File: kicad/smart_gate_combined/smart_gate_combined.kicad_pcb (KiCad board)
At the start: 2 copper layers, 250 x 150 mm, 35 parts

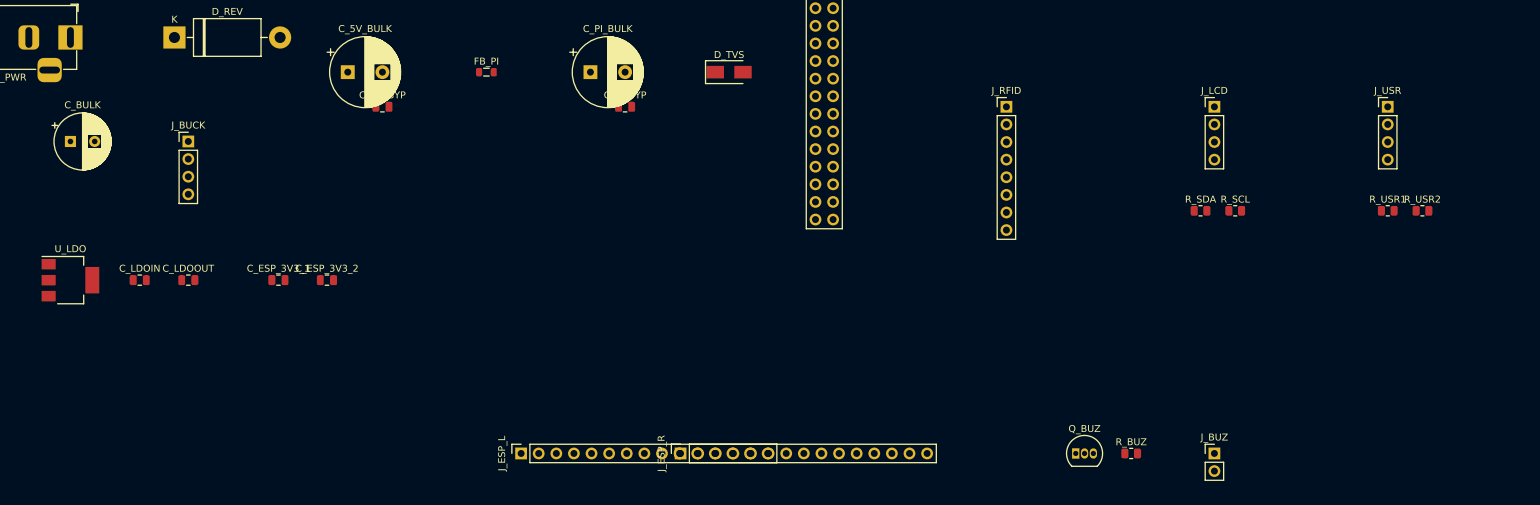
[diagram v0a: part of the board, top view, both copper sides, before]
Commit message: fix(kicad): Pi 4 target + all-THT footprints
Two clarifications from user 2026-05-22:
1. Hardware is Raspberry Pi 4 (not Pi 5 as previously assumed). GPIO layout
   identical, but power budget relaxed (1.5A peak vs 5A) and Pi 4 has no
   strict PMIC so GPIO-fed 5V is safer.
2. All discrete components must be through-hole (THT), not SMD — user does
   not have reflow/hot-air, prefers hand-soldering.

Changes:
- Spec §1, §2, decision log: Pi 5 -> Pi 4, buck 5A -> 3A, peak 3.6A -> 2.1A
- Spec §2: AMS1117 SOT-223 -> LM1117-3.3 TO-220
- Spec risks 6: Pi 4 tolerance noted (more forgiving than Pi 5)
- Spec decisions 23-24: THT preference + Pi 4 target documented
- SKiDL build_combined.py: all SMD footprints converted to THT
  (R 0805 -> Axial DIN0207, C 0805 -> Disc D5.0, D_SMA -> DO-15,
   AMS1117 -> LM1117-3.3 TO-220, L 0805 -> Axial Fastron)
- Regenerated netlist + PCB: 35 footprints, 0 ERC errors

Co-Authored-By: Claude Opus 4.7 <noreply@anthropic.com>
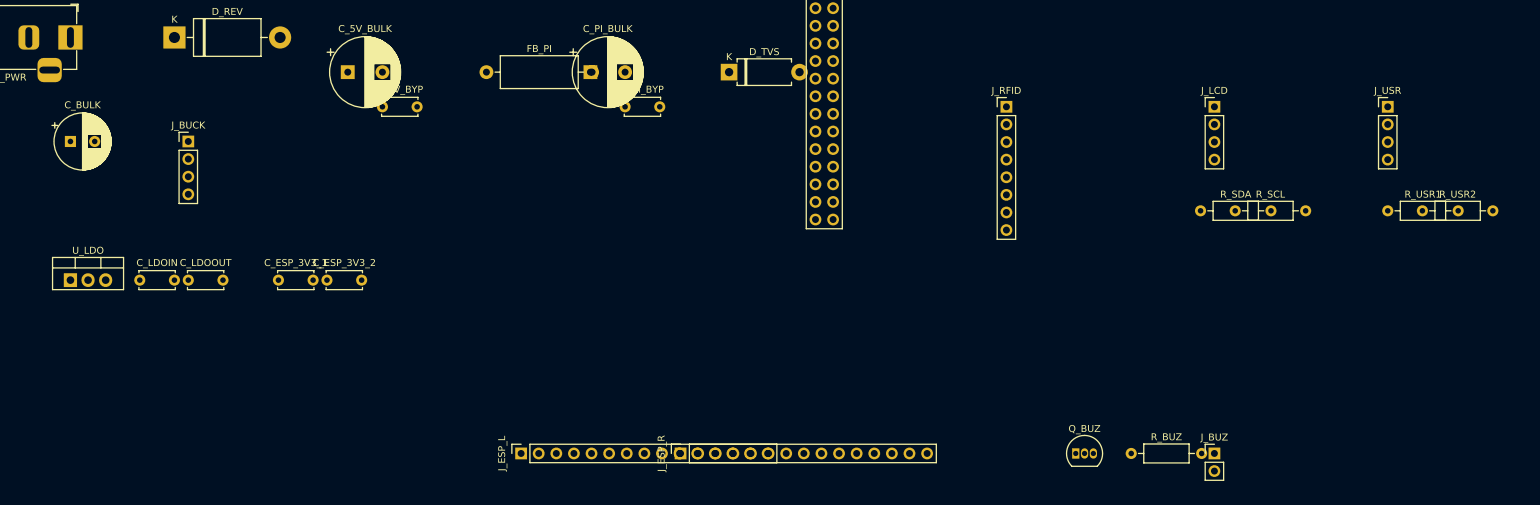
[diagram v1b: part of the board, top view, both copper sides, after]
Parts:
- removed the C_5V_BYP at (160.0, 150.0)
- removed the C_LDOIN at (125.0, 175.0)
- removed the C_LDOOUT at (132.0, 175.0)
- removed the C_PI_BYP at (195.0, 150.0)
- removed the D_TVS at (210.0, 145.0)
- removed the FB_PI at (175.0, 145.0)
- removed the R_BUZ at (268.0, 200.0)
- removed the R_SCL at (283.0, 165.0)
- removed the R_SDA at (278.0, 165.0)
- removed the U_LDO at (115.0, 175.0)
- added C_5V_BYP: 100nF, C_Disc_D5.0mm_W2.5mm_P5.00mm, F.Cu at (160.0, 150.0)
- added C_LDOIN: 10uF, C_Disc_D5.0mm_W2.5mm_P5.00mm, F.Cu at (125.0, 175.0)
- added C_LDOOUT: 10uF, C_Disc_D5.0mm_W2.5mm_P5.00mm, F.Cu at (132.0, 175.0)
- added C_PI_BYP: 100nF, C_Disc_D5.0mm_W2.5mm_P5.00mm, F.Cu at (195.0, 150.0)
- added D_TVS: SMAJ5.0A, D_DO-15_P10.16mm_Horizontal, F.Cu at (210.0, 145.0)
- added FB_PI: FB_600R_3A, L_Axial_L11.0mm_D4.5mm_P15.24mm_Horizontal_Fastron_MECC, F.Cu at (175.0, 145.0)
- added R_BUZ: 1k, R_Axial_DIN0207_L6.3mm_D2.5mm_P10.16mm_Horizontal, F.Cu at (268.0, 200.0)
- added R_SCL: 4.7k, R_Axial_DIN0207_L6.3mm_D2.5mm_P10.16mm_Horizontal, F.Cu at (283.0, 165.0)
- added R_SDA: 4.7k, R_Axial_DIN0207_L6.3mm_D2.5mm_P10.16mm_Horizontal, F.Cu at (278.0, 165.0)
- added U_LDO: LM1117-3.3, TO-220-3_Vertical, F.Cu at (115.0, 175.0)
- C_ESP_3V3_1, C_ESP_3V3_2: footprint C_0805_2012Metric -> C_Disc_D5.0mm_W2.5mm_P5.00mm
- R_USR1, R_USR2: footprint R_0805_2012Metric -> R_Axial_DIN0207_L6.3mm_D2.5mm_P10.16mm_Horizontal

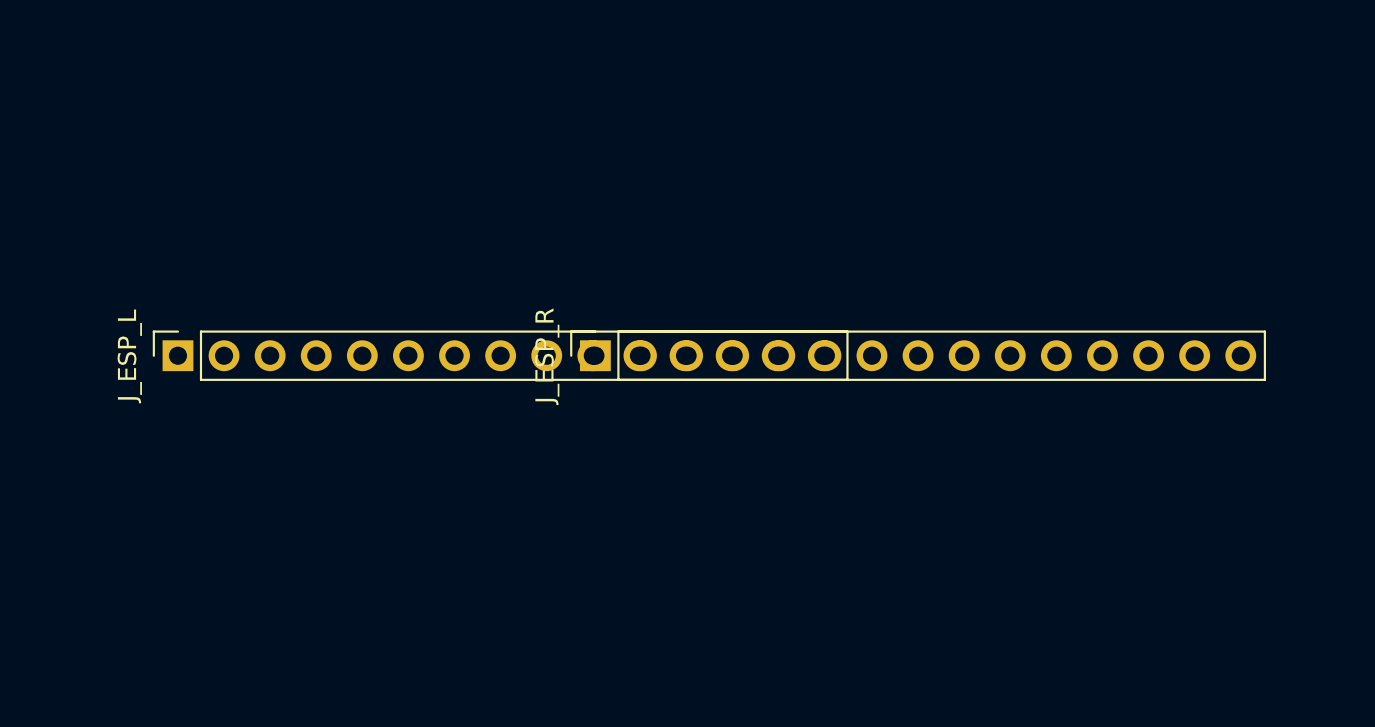
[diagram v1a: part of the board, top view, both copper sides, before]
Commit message: fix(kicad): single 2x15 ESP32 DevKit footprint, custom 25.4mm rail spacing
Replaced 2x Conn_01x15 sockets (J_ESP_L + J_ESP_R) with single
Conn_02x15_Odd_Even using a project-local custom footprint
ESP32_DevKit_V1_30pin (kicad/smart_gate_combined/footprints.pretty/).

Benefit: rail-to-rail spacing of 25.4mm guaranteed by the footprint itself,
not by separate footprint placements that could drift. DevKit will fit
exactly when soldered.

Pin numbering uses standard Conn_02x15_Odd_Even convention (odd = left
rail top-to-bottom, even = right rail top-to-bottom).

Also patched import_netlist.py to try the project-local footprints.pretty
directory before falling back to the system KiCad footprint library.

Co-Authored-By: Claude Opus 4.7 <noreply@anthropic.com>
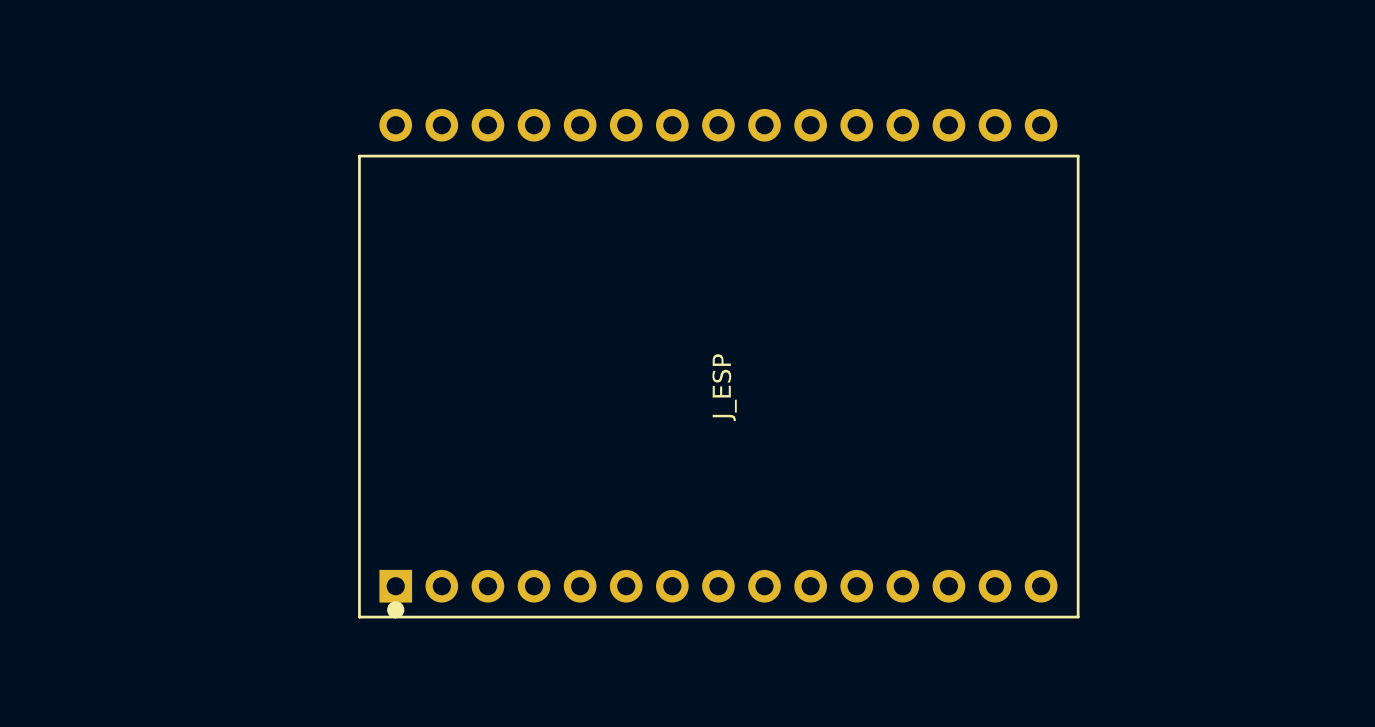
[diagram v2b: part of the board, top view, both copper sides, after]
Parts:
- removed J_ESP_L: DevKit_L, PinSocket_1x15_P2.54mm_Vertical
- removed J_ESP_R: DevKit_R, PinSocket_1x15_P2.54mm_Vertical
- added J_ESP: ESP32_DevKit_V1, ESP32_DevKit_V1_30pin, F.Cu at (192.0, 200.0)

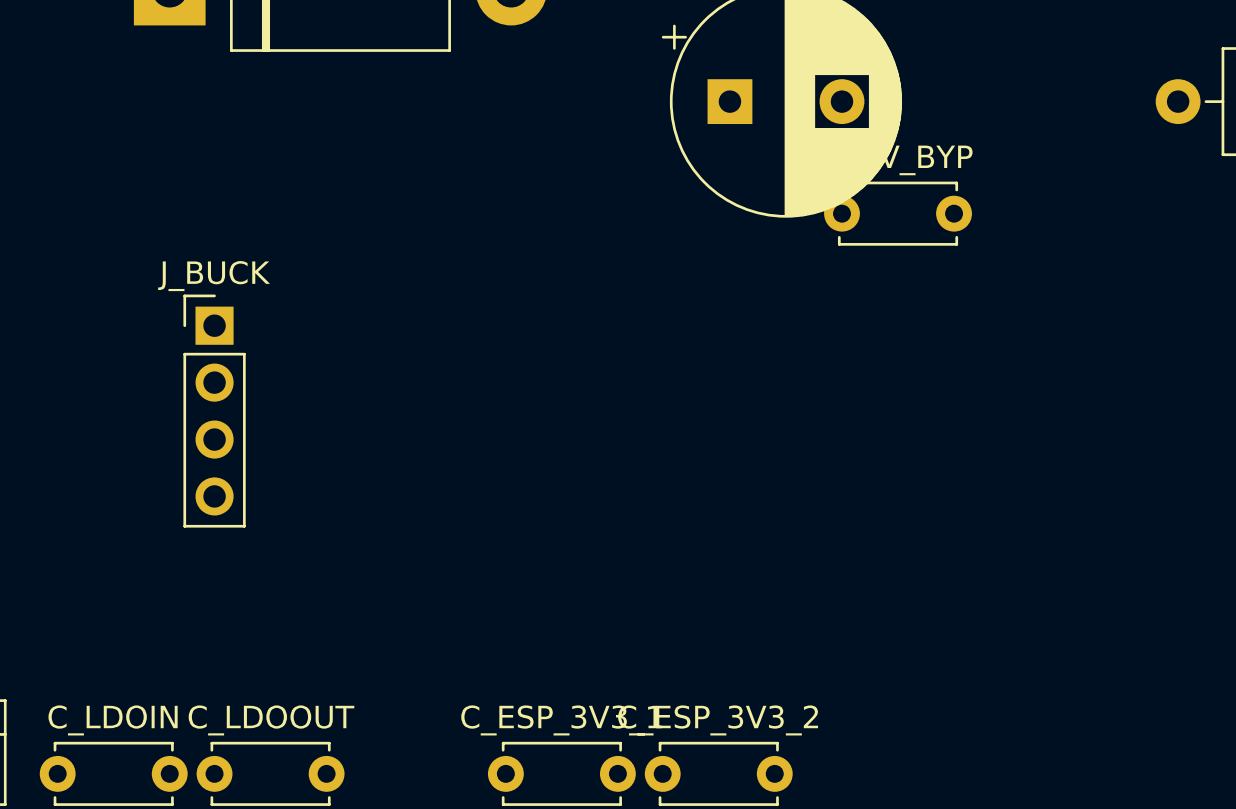
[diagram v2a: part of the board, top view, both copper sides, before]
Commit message: feat(kicad): LM2596 mini module custom footprint
Replaced generic 4-pin header for buck connection with custom footprint
LM2596_Mini_Buck matching the physical layout of the common ~43x21mm
LM2596 module sold in Vietnam:
  - 4 corner pads (not in-line)
  - IN pair on left, OUT pair on right (35mm apart)
  - V+ on top, GND on bottom (14mm apart)
  - 1.0mm drill, 2.0mm pad for wire-thick pins

User can solder the module directly onto the motherboard via the 4 corner
pads. If physical module dimensions differ, edit footprint pad coords.

Co-Authored-By: Claude Opus 4.7 <noreply@anthropic.com>
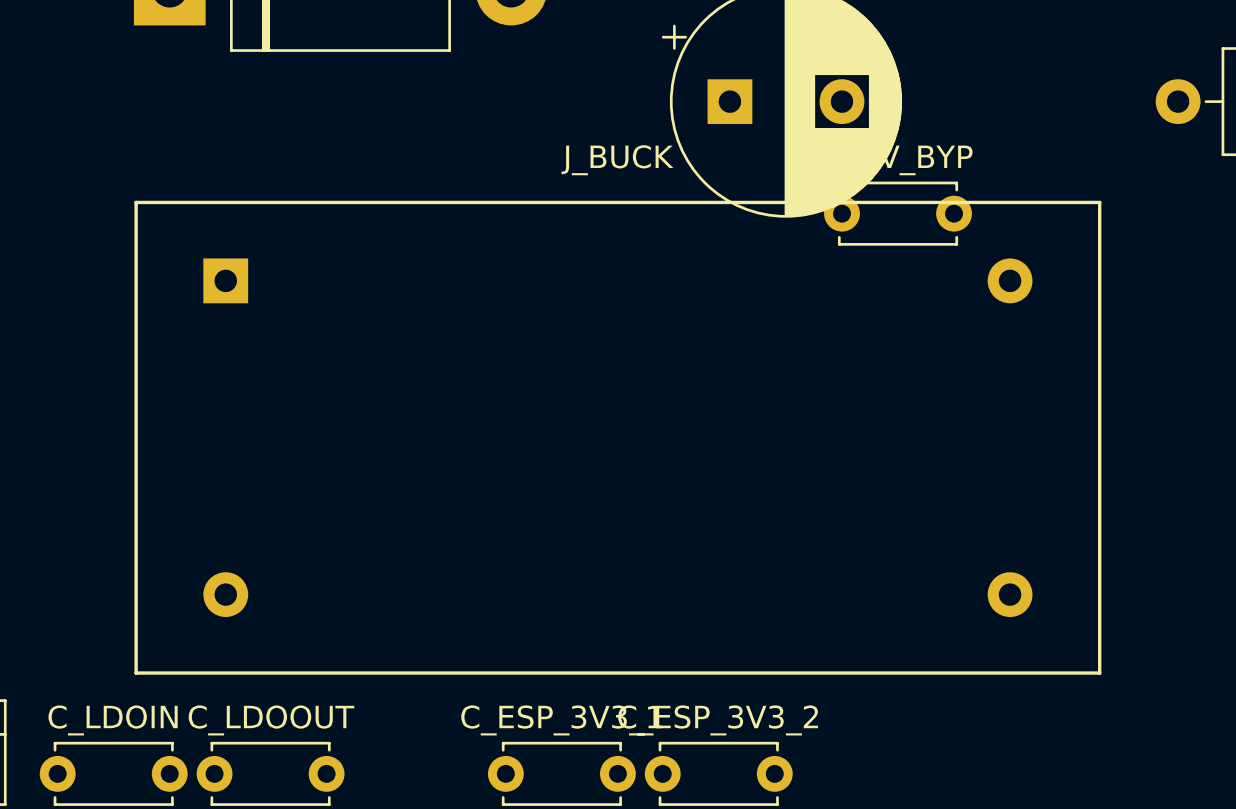
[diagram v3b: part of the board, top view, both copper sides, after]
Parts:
- removed the J_BUCK at (132.0, 155.0)
- added J_BUCK: LM2596_Mini_Buck, LM2596_Mini_Buck, F.Cu at (150.0, 160.0)

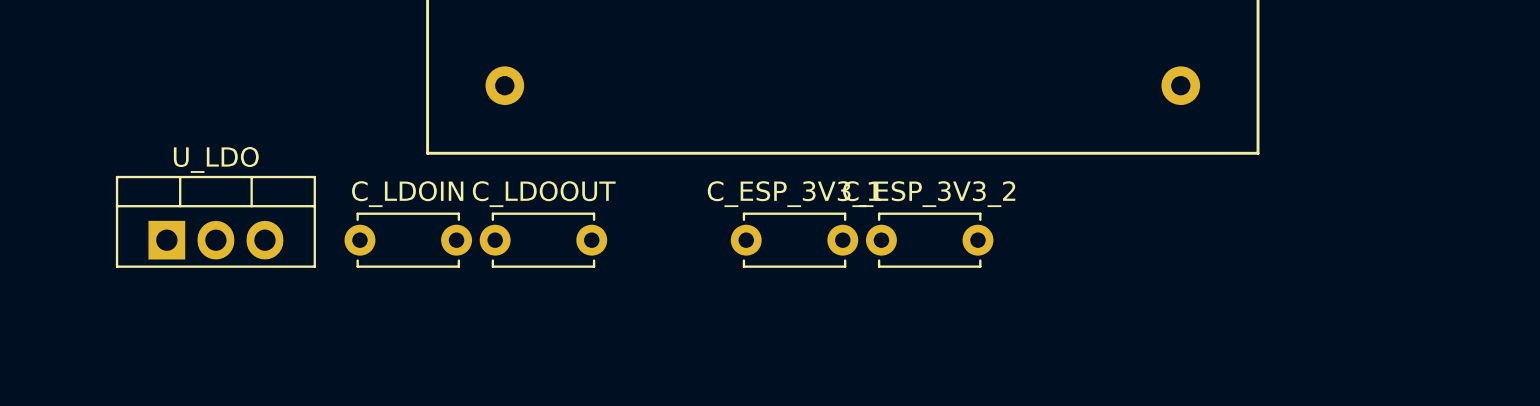
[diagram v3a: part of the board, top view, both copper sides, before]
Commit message: simplify(kicad): drop LM1117 — use ESP32 DevKit onboard 3V3 LDO
External 3.3V load is only ~31 mA (RC522 ~30 mA + LCD pull-ups ~1.4 mA),
well within the ESP32 DevKit's onboard AMS1117 budget (~500 mA after the
ESP32 chip's own ~150 mA). No need for a second LDO on the motherboard.

Removed:
- U_LDO (LM1117-3.3 in TO-220)
- C_LDOIN, C_LDOOUT (10 uF bypass caps)
- Placement coords for those refs

The +3V3 net is now driven by J_ESP pin 1 (DevKit 3V3 OUT).
RC522 VCC and LCD pull-ups attach to it as before.

Total footprints: 31 components + 4 mounts = 35 -> now 27 + 4 = 31.
Spec §2.2 updated accordingly.

Co-Authored-By: Claude Opus 4.7 <noreply@anthropic.com>
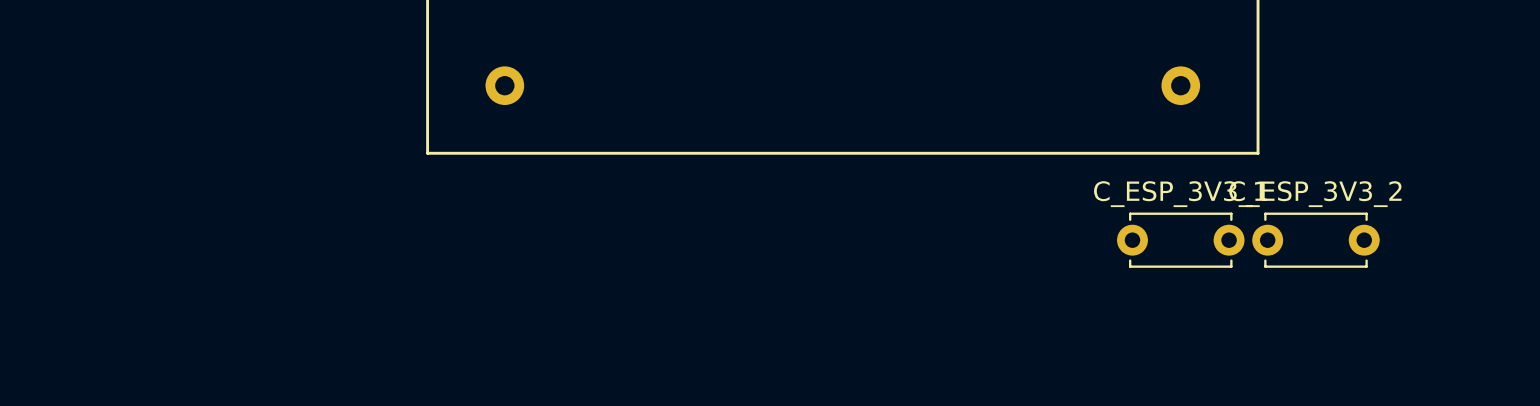
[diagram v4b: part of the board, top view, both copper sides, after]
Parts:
- removed C_LDOOUT: 10uF, C_Disc_D5.0mm_W2.5mm_P5.00mm
- removed the C_PI_BULK at (190.0, 145.0)
- removed U_LDO: LM1117-3.3, TO-220-3_Vertical
- C_PI_BULK: renamed from C_LDOIN; value 10uF -> 1000uF/10V; footprint C_Disc_D5.0mm_W2.5mm_P5.00mm -> CP_Radial_D10.0mm_P5.00mm
- moved C_PI_BULK 71.6 mm to (190.0, 145.0)
- moved C_ESP_3V3_1 20.0 mm to (165.0, 175.0)
- moved C_ESP_3V3_2 20.0 mm to (172.0, 175.0)
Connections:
- C_PI_BULK pad 1: +5V -> PI_5V_FILTERED

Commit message: feat(kicad): full autonomous PCB layout — routed, GND poured, gerbers
Pipeline (all Python-driven, no GUI clicks):
- autoroute.py: ExportSpecctraDSN -> FreeRouting 1.7 (Java 11 compat) -> SES
- import_ses.py: parse SES sexpr, add 356 PCB_TRACK segments to board
  (159 F.Cu + 197 B.Cu, no vias — all-THT pads bridge layers)
- add_gnd_pour.py: ZONE on B.Cu net GND, full board minus 0.5mm margin,
  filled via ZONE_FILLER
- export_gerbers.py: 9 layers (F/B Cu/Paste/Silk/Mask + Edge.Cuts) + drill file

FreeRouting reported 51.79%% optimization improvement after 23s.
All output committed: .dsn .ses smart_gate_combined.kicad_pcb gerber/*.gbr+drl

Co-Authored-By: Claude Opus 4.7 <noreply@anthropic.com>
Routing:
- net GND: track 0.00 -> 560.4 mm
- net +5V: track 0.00 -> 288.8 mm
- net +3V3: track 0.00 -> 257.8 mm
- net HCSR_ECHO_3V3: track 0.00 -> 140.6 mm
- net SERVO_PWM: track 0.00 -> 139.3 mm
- net HCSR_TRIG: track 0.00 -> 123.1 mm
- net RC522_MOSI: track 0.00 -> 108.0 mm
- net I2C_SCL: track 0.00 -> 105.3 mm
- net I2C_SDA: track 0.00 -> 105.1 mm
- net IO39: track 0.00 -> 90.2 mm
- net IO36: track 0.00 -> 86.6 mm
- net RC522_SCK: track 0.00 -> 81.5 mm
- net RC522_MISO: track 0.00 -> 75.8 mm
- net RC522_CS: track 0.00 -> 65.6 mm
- net PI_TX_ESP_RX: track 0.00 -> 64.5 mm
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- added copper zone on B.Cu, net GND
